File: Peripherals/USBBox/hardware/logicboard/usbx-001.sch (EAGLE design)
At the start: 3 parts, among them J2 AUDIO_JACK_TRRSSMD_RA

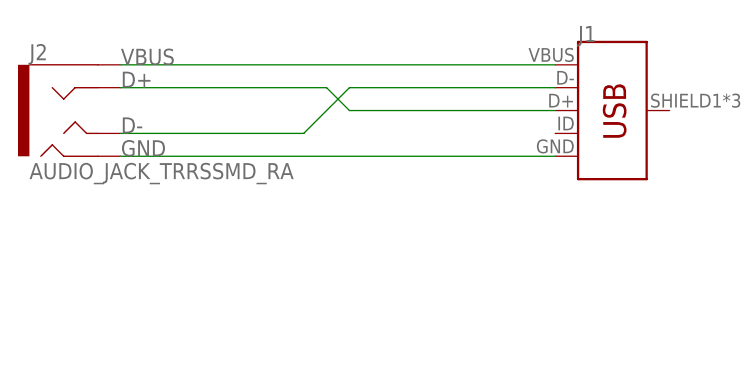
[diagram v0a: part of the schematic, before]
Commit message: Added resistors for iPod shuffle compatibility.
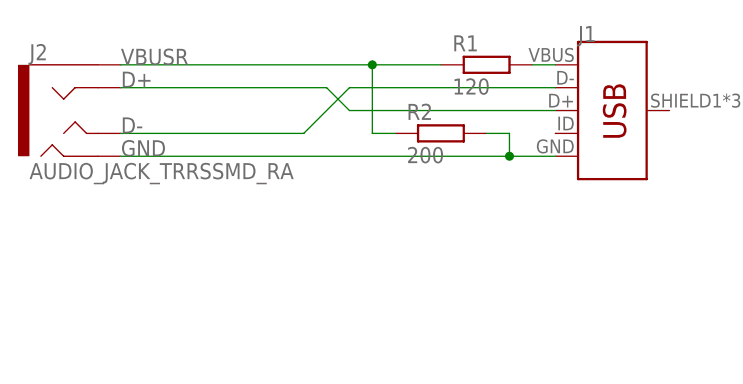
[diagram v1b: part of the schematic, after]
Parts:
- added R1: 120, rcl:R-EU_R2012
- added R2: 200, rcl:R-EU_R2012
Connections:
- new net VBUSR: J2.EARTH, R1.1, R2.1
- net GND: now also R2.2
- net VBUS: now also R1.2; no longer J2.EARTH
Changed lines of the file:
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@@
 <part name="J1" library="SparkFun-Connectors" library_urn="urn:adsk.eagle:library:513" deviceset="USB_MICRO-B" device="_FEMALE-SMT" package3d_urn="urn:adsk.eagle:package:38238/1"/>
 <part name="J2" library="SparkFun-Connectors" library_urn="urn:adsk.eagle:library:513" deviceset="AUDIO_JACK_TRRS" device="SMD_RA" package3d_urn="urn:adsk.eagle:package:38268/1"/>
+<part name="R1" library="rcl" library_urn="urn:adsk.eagle:library:334" deviceset="R-EU_" device="R2012" package3d_urn="urn:adsk.eagle:package:23543/2" value="120"/>
+<part name="R2" library="rcl" library_urn="urn:adsk.eagle:library:334" deviceset="R-EU_" device="R2012" package3d_urn="urn:adsk.eagle:package:23543/2" value="200"/>
 </parts>
 <sheets>
@@
 <attribute name="VALUE" x="119.38" y="76.2" size="1.778" layer="96" font="vector"/>
 </instance>
+<instance part="R1" gate="G$1" x="170.18" y="88.9" smashed="yes">
+<attribute name="NAME" x="166.37" y="90.3986" size="1.778" layer="95"/>
+<attribute name="VALUE" x="166.37" y="85.598" size="1.778" layer="96"/>
+</instance>
+<instance part="R2" gate="G$1" x="165.1" y="81.28" smashed="yes">
+<attribute name="NAME" x="161.29" y="82.7786" size="1.778" layer="95"/>
+<attribute name="VALUE" x="161.29" y="77.978" size="1.778" layer="96"/>
+</instance>
 </instances>
 <busses>
 </busses>
 <nets>
-<net name="VBUS" class="2">
-<segment>
-<pinref part="J1" gate="G$1" pin="VBUS"/>
-<pinref part="J2" gate="G$1" pin="EARTH"/>
-<wire x1="177.8" y1="88.9" x2="129.54" y2="88.9" width="0.1524" layer="91"/>
-<label x="129.54" y="88.9" size="1.778" layer="95"/>
-</segment>
-</net>
 <net name="D-" class="0">
 <segment>
@@
 <pinref part="J1" gate="G$1" pin="GND"/>
 <pinref part="J2" gate="G$1" pin="RING2"/>
-<wire x1="177.8" y1="78.74" x2="129.54" y2="78.74" width="0.1524" layer="91"/>
+<wire x1="177.8" y1="78.74" x2="172.72" y2="78.74" width="0.1524" layer="91"/>
 <label x="129.54" y="78.74" size="1.778" layer="95"/>
+<pinref part="R2" gate="G$1" pin="2"/>
+<wire x1="172.72" y1="78.74" x2="129.54" y2="78.74" width="0.1524" layer="91"/>
+<wire x1="170.18" y1="81.28" x2="172.72" y2="81.28" width="0.1524" layer="91"/>
+<wire x1="172.72" y1="81.28" x2="172.72" y2="78.74" width="0.1524" layer="91"/>
+<junction x="172.72" y="78.74"/>
+</segment>
+</net>
+<net name="VBUS" class="2">
+<segment>
+<pinref part="J1" gate="G$1" pin="VBUS"/>
+<pinref part="R1" gate="G$1" pin="2"/>
+<wire x1="177.8" y1="88.9" x2="175.26" y2="88.9" width="0.1524" layer="91"/>
+</segment>
+</net>
+<net name="VBUSR" class="2">
+<segment>
+<pinref part="R1" gate="G$1" pin="1"/>
+<pinref part="J2" gate="G$1" pin="EARTH"/>
+<wire x1="165.1" y1="88.9" x2="157.48" y2="88.9" width="0.1524" layer="91"/>
+<label x="129.54" y="88.9" size="1.778" layer="95"/>
+<wire x1="157.48" y1="88.9" x2="129.54" y2="88.9" width="0.1524" layer="91"/>
+<wire x1="157.48" y1="88.9" x2="157.48" y2="81.28" width="0.1524" layer="91"/>
+<junction x="157.48" y="88.9"/>
+<pinref part="R2" gate="G$1" pin="1"/>
+<wire x1="157.48" y1="81.28" x2="160.02" y2="81.28" width="0.1524" layer="91"/>
 </segment>
 </net>
@@
 packages will not be understood (or retained) with this version.
 </note>
+<note version="8.4" severity="warning">
+Since Version 8.4, EAGLE supports properties for SPICE simulation.
+Probes in schematics and SPICE mapping objects found in parts and library devices
+will not be understood with this version. Update EAGLE to the latest version
+for full support of SPICE simulation.
+</note>
 </compatibility>
